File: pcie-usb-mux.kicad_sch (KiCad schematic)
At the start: 0 parts

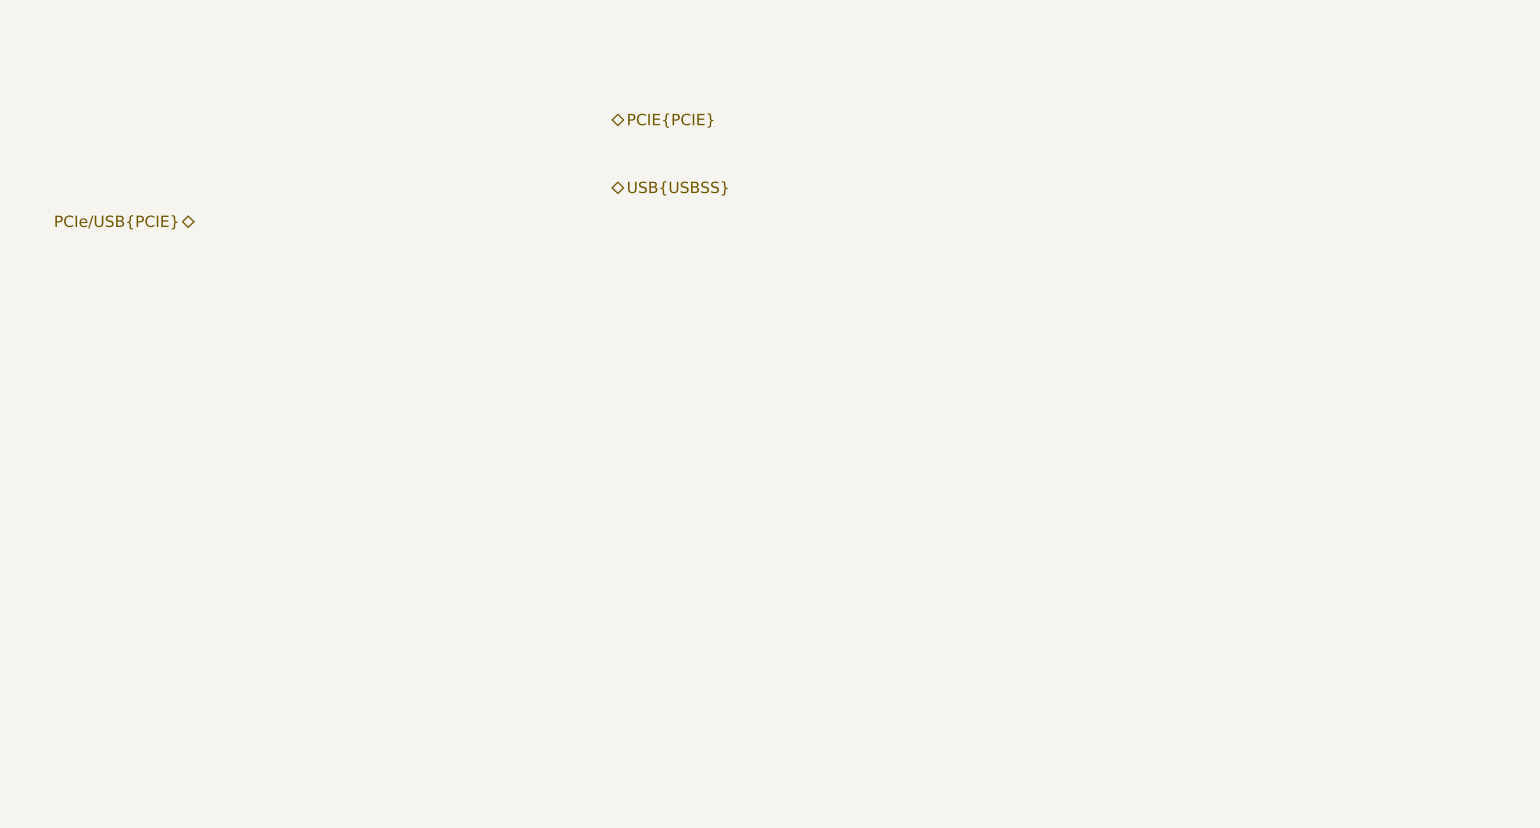
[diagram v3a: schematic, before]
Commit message: [#82176] Place PCIe/USB mux
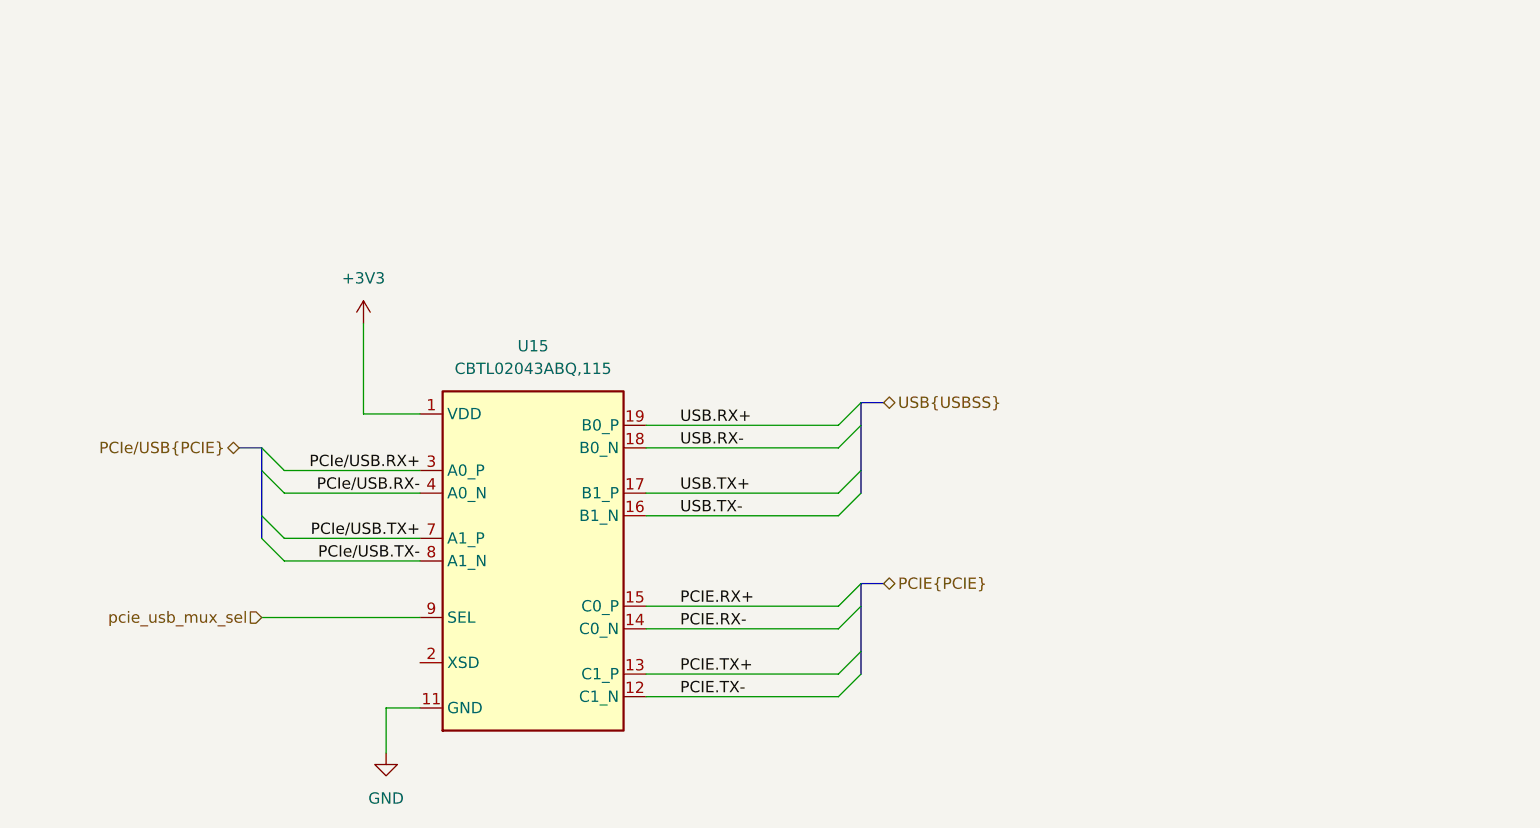
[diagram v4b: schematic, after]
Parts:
- added U15: CBTL02043ABQ, antmicro-footprints:DHVQFN-20-1EP_2.5x4.5_P0.5mm, symbol antmicroLogicSignalSwitchesMultiplexersDecoders:CBTL02043ABQ
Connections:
- new net +3V3: U15.1 (VDD), U15.10 (VDD), U15.6 (VDD)
- new net GND: U15.11 (GND), U15.20 (GND), U15.21 (GND), U15.5 (GND)
- new net PCIE.RX+: U15.15 (C0_P)
- new net PCIE.RX-: U15.14 (C0_N)
- new net PCIE.TX+: U15.13 (C1_P)
- new net PCIE.TX-: U15.12 (C1_N)
- new net PCIe/USB.RX+: U15.3 (A0_P)
- new net PCIe/USB.RX-: U15.4 (A0_N)
- new net PCIe/USB.TX+: U15.7 (A1_P)
- new net PCIe/USB.TX-: U15.8 (A1_N)
- new net USB.RX+: U15.19 (B0_P)
- new net USB.RX-: U15.18 (B0_N)
- new net USB.TX+: U15.17 (B1_P)
- new net USB.TX-: U15.16 (B1_N)
- new net pcie_usb_mux_sel: U15.9 (SEL)

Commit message: [#82176] Add passives to PCIe/USB mux
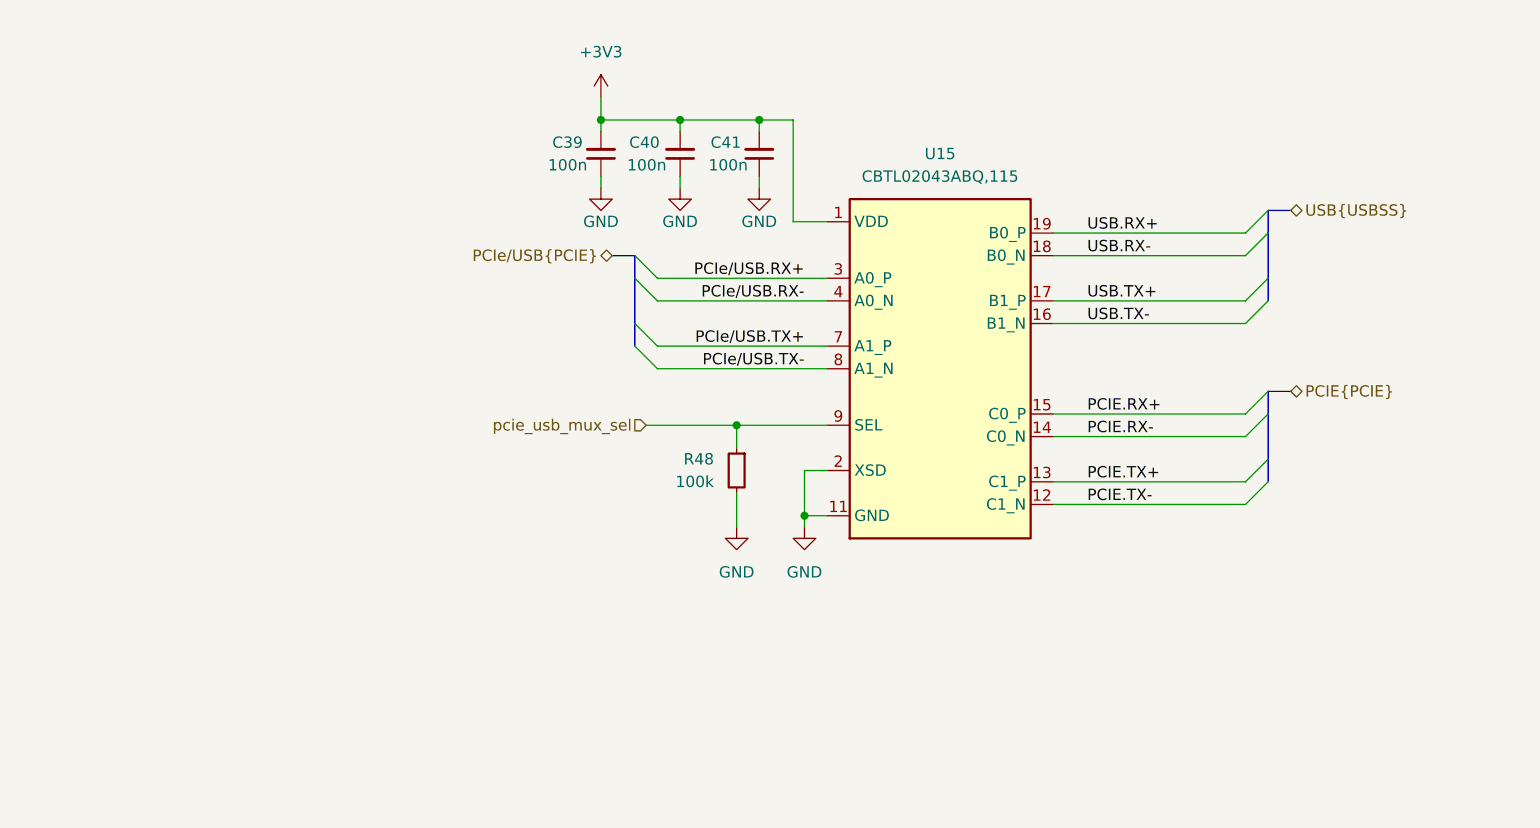
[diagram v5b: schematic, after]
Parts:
- added C39, C40, C41: C_100n_0402, antmicro-footprints:C_0402_1005Metric, symbol antmicroCapacitors0402:C_100n_0402
- added R48: R_100k_0402, antmicro-footprints:R_0402_1005Metric, symbol antmicroResistors0402:R_100k_0402
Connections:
- net +3V3: now also C39.2, C40.2, C41.2
- net GND: now also U15.2 (XSD), C39.1, C40.1, C41.1, R48.2
- net pcie_usb_mux_sel: now also R48.1
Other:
- moved on the sheet: U15

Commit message: [#82148] Replace PCIe/USB mux with TMUXHS4212IRKSR
Update PCIe/USB mux sheet
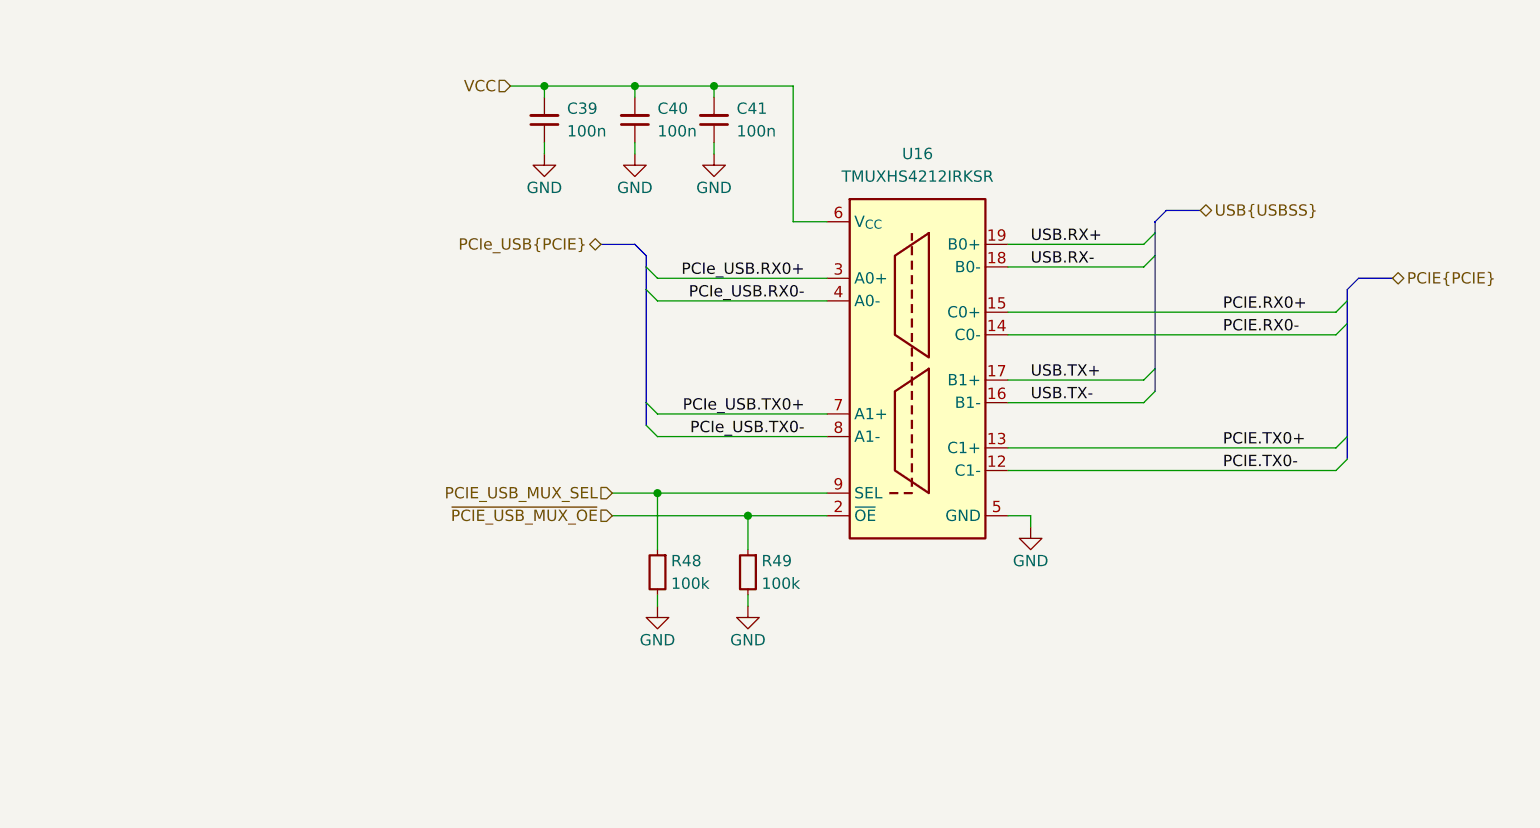
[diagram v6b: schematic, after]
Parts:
- removed U15: CBTL02043ABQ, antmicro-footprints:DHVQFN-20-1EP_2.5x4.5_P0.5mm, symbol antmicroLogicSignalSwitchesMultiplexersDecoders:CBTL02043ABQ
- added R49: R_100k_0402, antmicro-footprints:R_0402_1005Metric, symbol antmicroResistors0402:R_100k_0402
- added U16: TMUXHS4212IRKSR, antmicro-footprints:VQFN-20_1EP_4.5x2.5mm_P0.5mm, symbol antmicroInterfaceAnalogSwitchesSpecialPurpose:TMUXHS4212IRKSR
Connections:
- net GND: now also R49.2, U16.11 (GND), U16.20 (GND), U16.21 (GND), U16.5 (GND)
- net USB.RX+: now also U16.19 (B0+)
- net USB.RX-: now also U16.18 (B0-)
- net USB.TX+: now also U16.17 (B1+)
- net USB.TX-: now also U16.16 (B1-)
- net +3V3 renamed VCC
- net VCC: now also U16.6 (V_{CC})
- net pcie_usb_mux_sel renamed PCIE_USB_MUX_SEL
- net PCIE_USB_MUX_SEL: now also U16.9 (SEL)
- new net PCIE.RX0+: U16.15 (C0+)
- new net PCIE.RX0-: U16.14 (C0-)
- new net PCIE.TX0+: U16.13 (C1+)
- new net PCIE.TX0-: U16.12 (C1-)
- new net PCIe_USB.RX0+: U16.3 (A0+)
- new net PCIe_USB.RX0-: U16.4 (A0-)
- new net PCIe_USB.TX0+: U16.7 (A1+)
- new net PCIe_USB.TX0-: U16.8 (A1-)
- new net ~{PCIE_USB_MUX_OE}: R49.1, U16.2 (~{OE})
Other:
- moved on the sheet: C39, C40, C41, R48

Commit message: [#83337] Finalized PCIe-SGMII mux and PCIe-USB mux
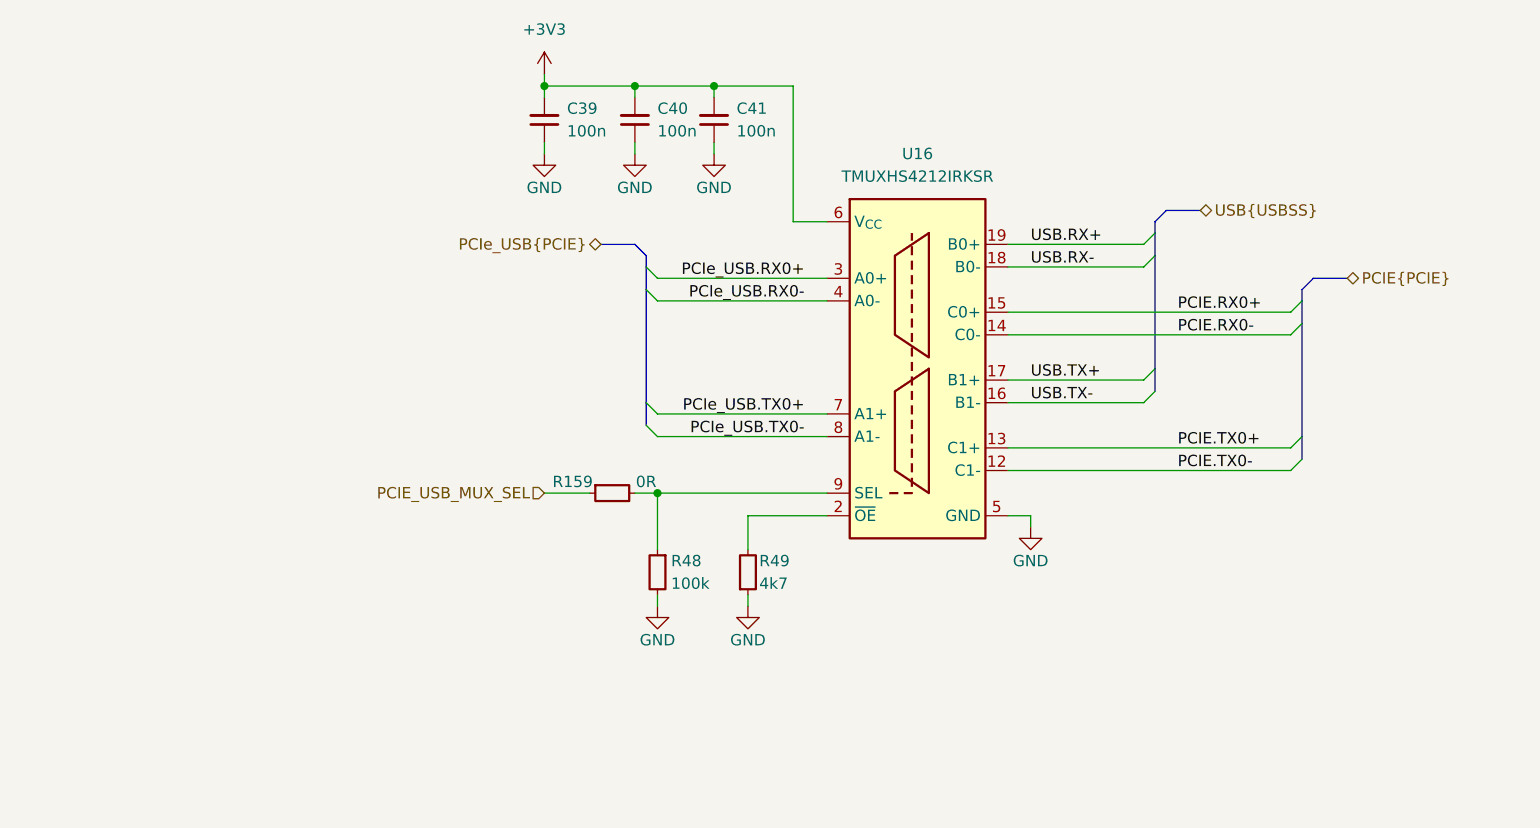
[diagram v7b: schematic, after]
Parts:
- removed R49: R_100k_0402, antmicro-footprints:R_0402_1005Metric, symbol antmicroResistors0402:R_100k_0402
- added R159: R_0R_0402, antmicro-footprints:R_0402_1005Metric, symbol antmicroResistors0402:R_0R_0402
- added R49: R_4k7_0402, antmicro-footprints:R_0402_1005Metric, symbol antmicroResistors0402:R_4k7_0402
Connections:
- net GND: now also R49.1
- net PCIE_USB_MUX_SEL: now also R159.1; no longer R48.1, U16.9 (SEL)
- net VCC renamed +3V3
- net ~{PCIE_USB_MUX_OE}: no longer names the net of U16.2 (~{OE})
- net ~{PCIE_USB_MUX_OE}: now also R49.2
- new net: R159.2, R48.1, U16.9 (SEL)

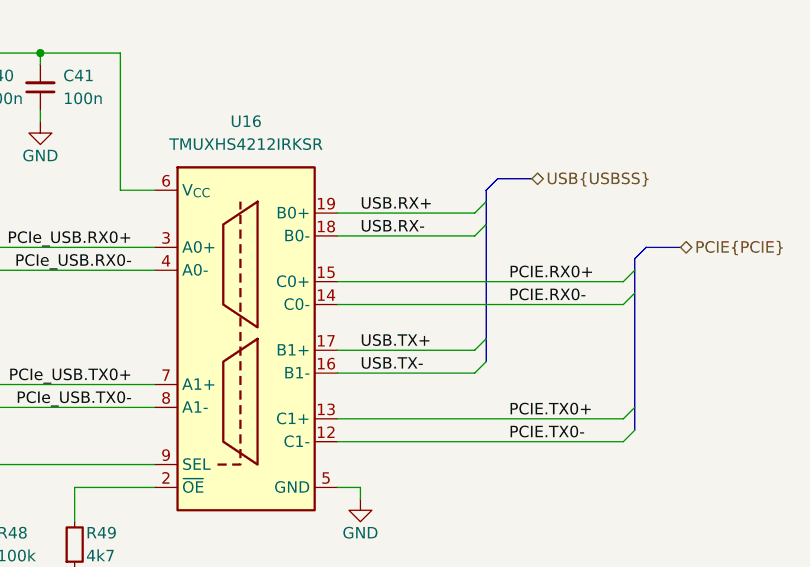
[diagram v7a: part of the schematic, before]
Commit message: [#83338] Fixed HS connection AC caps and TX/RX swaps
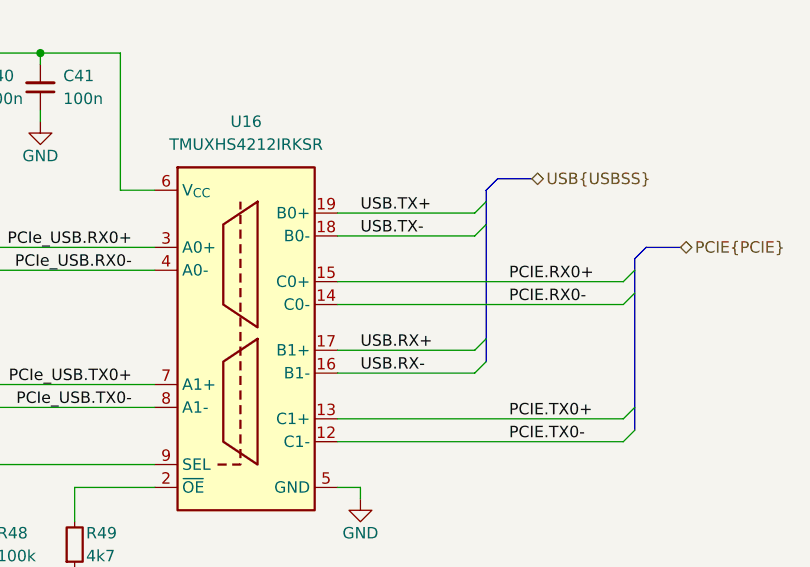
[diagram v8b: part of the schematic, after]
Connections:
- net USB.RX+: now also U16.17 (B1+); no longer U16.19 (B0+)
- net USB.RX-: now also U16.16 (B1-); no longer U16.18 (B0-)
- net USB.TX+: now also U16.19 (B0+); no longer U16.17 (B1+)
- net USB.TX-: now also U16.18 (B0-); no longer U16.16 (B1-)
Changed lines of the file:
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@@
 	)
 	(label "USB.TX-"
-		(at 222.25 133.35 0)
+		(at 222.25 118.11 0)
 		(effects
 			(font
@@
 	)
 	(label "USB.RX-"
-		(at 222.25 118.11 0)
+		(at 222.25 133.35 0)
 		(effects
 			(font
@@
 	)
 	(label "USB.RX+"
-		(at 222.25 115.57 0)
+		(at 222.25 130.81 0)
 		(effects
 			(font
@@
 	)
 	(label "USB.TX+"
-		(at 222.25 130.81 0)
+		(at 222.25 115.57 0)
 		(effects
 			(font
